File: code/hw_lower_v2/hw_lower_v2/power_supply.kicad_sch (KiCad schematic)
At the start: 34 parts, among them J14 Conn_01x02, U5 ICL7660A, U6 AMS1117, U7 AMS1117

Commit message: have one project part library
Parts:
- C12: footprint JLCPCB:CAP-TH_L18.0-W7.0-P15.00-D0.7 -> multi_new:CAP-TH_L18.0-W7.0-P15.00-D0.7
- F1: footprint JLCPCB:F1206 -> multi_new:F1206
- RV1: footprint JLCPCB:RES-TH_L12.5-W4.4-P7.50-D0.8-S3.60 -> multi_new:RES-TH_L12.5-W4.4-P7.50-D0.8-S3.60
- U5: footprint JLCPCB:SOIC-8_L5.0-W4.0-P1.27-LS6.0-BL -> multi_new:SOIC-8_L5.0-W4.0-P1.27-LS6.0-BL
- U6, U7: footprint JLCPCB:SOT-223_L6.7-W3.5-P2.30-BR -> multi_new:SOT-223_L6.7-W3.5-P2.30-BR

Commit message: finish 3d models
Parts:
- C12: footprint multi_new:CAP-TH_L18.0-W7.0-P15.00-D0.7 -> multi_new:CAP-TH_L13.0-W6.0-P10.00-D0.6; LCSC C914484 -> C489079
- J14: now left out of the parts list
- PS1: LCSC C2923575 -> C209908
- U7: symbol Regulator_Linear:AMS1117 -> multi_new:AMS1117
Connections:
- net at C19.1, JP4.2 (B), R38.2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: now also U6.4 (VO)
- net at C20.1, JP5.2 (B), R40.2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: now also U7.4 (VO)
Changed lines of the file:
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@@
 	)
 	(junction
+		(at 214.63 83.82)
+		(diameter 0)
+		(color 0 0 0 0)
+	)
+	(junction
 		(at 218.44 41.91)
 		(diameter 0)
@@
 	)
 	(junction
+		(at 214.63 41.91)
+		(diameter 0)
+		(color 0 0 0 0)
+	)
+	(junction
 		(at 119.38 88.9)
 		(diameter 0)
@@
 	(wire
 		(pts
+			(xy 213.36 86.36) (xy 214.63 86.36)
+		)
+		(stroke
+			(width 0)
+			(type default)
+		)
+	)
+	(wire
+		(pts
 			(xy 195.58 53.34) (xy 195.58 58.42)
 		)
@@
 	(wire
 		(pts
+			(xy 214.63 83.82) (xy 214.63 86.36)
+		)
+		(stroke
+			(width 0)
+			(type default)
+		)
+	)
+	(wire
+		(pts
 			(xy 86.36 88.9) (xy 87.63 88.9)
 		)
@@
 	(wire
 		(pts
+			(xy 214.63 41.91) (xy 214.63 44.45)
+		)
+		(stroke
+			(width 0)
+			(type default)
+		)
+	)
+	(wire
+		(pts
 			(xy 226.06 58.42) (xy 218.44 58.42)
 		)
@@
 	(wire
 		(pts
+			(xy 213.36 44.45) (xy 214.63 44.45)
+		)
+		(stroke
+			(width 0)
+			(type default)
+		)
+	)
+	(wire
+		(pts
 			(xy 195.58 100.33) (xy 205.74 100.33)
 		)
@@
 	(wire
 		(pts
+			(xy 214.63 41.91) (xy 218.44 41.91)
+		)
+		(stroke
+			(width 0)
+			(type default)
+		)
+	)
+	(wire
+		(pts
 			(xy 97.79 111.76) (xy 97.79 110.49)
 		)
@@
 	(wire
 		(pts
+			(xy 214.63 83.82) (xy 218.44 83.82)
+		)
+		(stroke
+			(width 0)
+			(type default)
+		)
+	)
+	(wire
+		(pts
 			(xy 195.58 83.82) (xy 198.12 83.82)
 		)
@@
 	(wire
 		(pts
-			(xy 213.36 41.91) (xy 218.44 41.91)
+			(xy 213.36 41.91) (xy 214.63 41.91)
 		)
 		(stroke
@@
 	(wire
 		(pts
-			(xy 213.36 83.82) (xy 218.44 83.82)
+			(xy 213.36 83.82) (xy 214.63 83.82)
 		)
 		(stroke
@@
 			)
 		)
-		(property "Footprint" "multi_new:CAP-TH_L18.0-W7.0-P15.00-D0.7"
+		(property "Footprint" "multi_new:CAP-TH_L13.0-W6.0-P10.00-D0.6"
 			(at 65.7352 46.99 0)
 			(effects
@@
 			)
 		)
-		(property "LCSC" "C914484"
+		(property "LCSC" "C489079"
 			(at 64.77 43.18 0)
 			(effects
@@
 		(unit 1)
 		(exclude_from_sim no)
-		(in_bom yes)
+		(in_bom no)
 		(on_board yes)
 		(dnp no)
@@
 	)
 	(symbol
-		(lib_id "Regulator_Linear:AMS1117")
+		(lib_id "multi_new:AMS1117")
 		(at 205.74 83.82 0)
 		(unit 1)
@@
 		(pin "2"
 		)
+		(pin "4"
+		)
 		(instances
 			(project "hw_lower_v2"
@@
 			)
 		)
-		(property "LCSC" "C2923575"
+		(property "LCSC" "C209908"
 			(at 82.55 43.18 0)
 			(effects
@@
 	)
 	(symbol
+		(lib_name "AMS1117_1")
 		(lib_id "Regulator_Linear:AMS1117")
 		(at 205.74 41.91 0)
@@
 		(pin "2"
 		)
+		(pin "4"
+		)
 		(instances

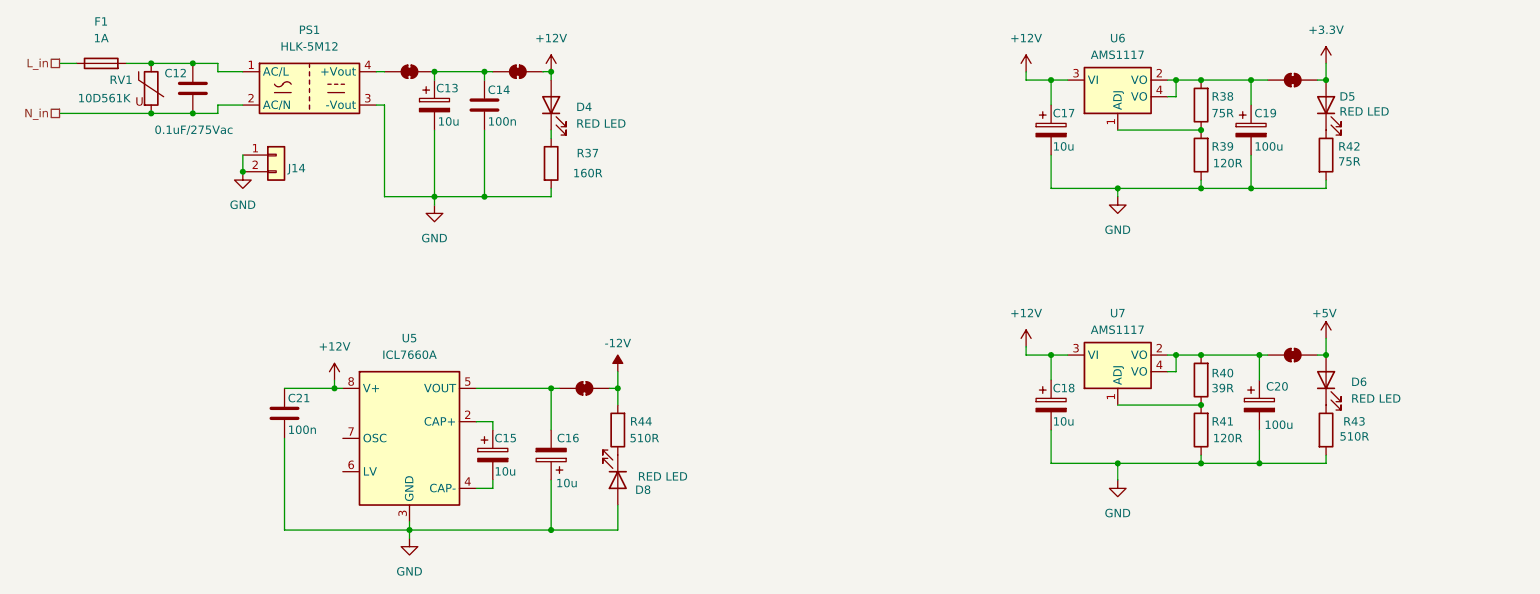
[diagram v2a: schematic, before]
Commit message: simplify component values
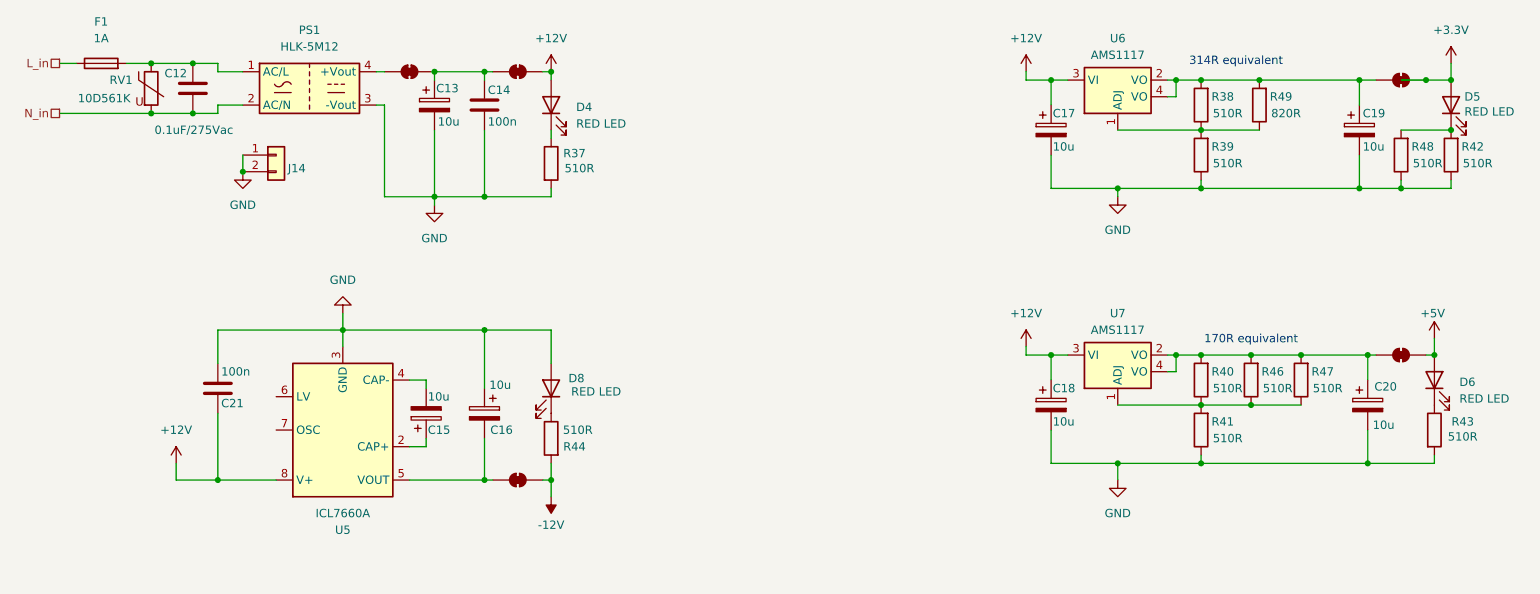
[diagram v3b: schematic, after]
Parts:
- added R46, R47, R48: 510R, Resistor_SMD:R_0603_1608Metric, symbol Device:R
- added R49: 820R, Resistor_SMD:R_0603_1608Metric, symbol Device:R
- C14, C21: LCSC C38141 -> C327162
- C19, C20: value 100u -> 10u; footprint Capacitor_SMD:CP_Elec_6.3x5.4 -> Capacitor_SMD:CP_Elec_4x5.4; LCSC C5138965 -> C72485
- R37: value 160R -> 510R; LCSC C22814 -> C23193
- R38, R42: value 75R -> 510R; LCSC C112309 -> C23193
- R39, R41: value 120R -> 510R; LCSC C125925 -> C23193
- R40: value 39R -> 510R; LCSC C137733 -> C23193
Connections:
- net GND: now also R42.1, R48.1; no longer R42.2
- net at C19.1, JP4.2 (B), R38.2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: now also R49.2
- net at R38.1, R39.2, U6.1 (ADJ): now also R49.1
- net at D5.1 (K): now also R42.2, R48.2; no longer R42.1
- net at R40.1, R41.2, U7.1 (ADJ): now also R46.1, R47.1
- net at C20.1, JP5.2 (B), R40.2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: now also R46.2, R47.2
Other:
- note added: "170R equivalent"
- note added: "314R equivalent"
- moved on the sheet: C15, C16, C19, C20, C21, D5, D6, D8, R43, R44, U5

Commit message: made a full reposition of the whole pcb. When I get everything working, the milkv module can be on the bottom pcb and all the device specific devices can be on the other pcb. Also now conceptualy, the current board can be broken onto two, and be made into a thin long one
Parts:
- removed JP2: SolderJumper_2_Bridged, Jumper:SolderJumper-2_P1.3mm_Bridged2Bar_RoundedPad1.0x1.5mm, symbol Jumper:SolderJumper_2_Bridged
- removed R38, R39, R40, R41, R46, R47: 510R, Resistor_SMD:R_0603_1608Metric, symbol Device:R
- removed R49: 820R, Resistor_SMD:R_0603_1608Metric, symbol Device:R
- removed U6: AMS1117, multi_new:SOT-223_L6.7-W3.5-P2.30-BR, symbol Regulator_Linear:AMS1117
- removed U7: AMS1117, multi_new:SOT-223_L6.7-W3.5-P2.30-BR, symbol multi_new:AMS1117
- added U6: AMS1117-33, multi_new:SOT-223_L6.7-W3.5-P2.30-BR, symbol multi_new:AMS1117-33
- added U7: AMS1117-5, multi_new:SOT-223_L6.7-W3.5-P2.30-BR, symbol multi_new:AMS1117-5
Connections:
- net +12V: now also U6.3 (VI), U7.3 (VI)
- net -12V: now also D8.1 (K); no longer R44.2
- net GND: now also R44.1, U6.1 (GND), U7.1 (GND); no longer D8.2 (A)
- net at C19.1, JP4.2 (B): now also U6.2 (VO), U6.4 (VO)
- net at C13.1, C14.1, JP1.2 (B): now also PS1.4 (+Vout)
- net at C20.1, JP5.2 (B): now also U7.2 (VO), U7.4 (VO)
- new net: D8.2 (A), R44.2
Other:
- note removed: "170R equivalent"
- note removed: "314R equivalent"
- moved on the sheet: C19, C20, D5, D6, D8, R42, R43, R44, R48

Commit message: add JLCPCB tooling holes and simplify further
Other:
- title: EVSE -> BlueEVSE
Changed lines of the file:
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@@
 	(paper "A4")
 	(title_block
-		(title "EVSE")
+		(title "BlueEVSE")
 		(date "2024-07-14")
 		(rev "V2")

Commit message: wip
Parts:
- C13, C15, C16, C17, C18, C19, C20: LCSC C72485 -> C86602
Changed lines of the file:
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@@
 			)
 		)
-		(property "LCSC" "C72485"
+		(property "LCSC" "C86602"
 			(at 100.33 92.71 0)
 			(effects
@@
 			)
 		)
-		(property "LCSC" "C72485"
+		(property "LCSC" "C86602"
 			(at 217.17 49.53 0)
 			(effects
@@
 			)
 		)
-		(property "LCSC" "C72485"
+		(property "LCSC" "C86602"
 			(at 195.58 49.53 0)
 			(effects
@@
 			)
 		)
-		(property "LCSC" "C72485"
+		(property "LCSC" "C86602"
 			(at 101.6 45.72 0)
 			(effects
@@
 			)
 		)
-		(property "LCSC" "C72485"
+		(property "LCSC" "C86602"
 			(at 195.58 91.44 0)
 			(effects
@@
 			)
 		)
-		(property "LCSC" "C72485"
+		(property "LCSC" "C86602"
 			(at 109.22 92.71 0)
 			(effects
@@
 			)
 		)
-		(property "LCSC" "C72485"
+		(property "LCSC" "C86602"
 			(at 220.98 91.44 0)
 			(effects
